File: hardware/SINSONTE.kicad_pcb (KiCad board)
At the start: 2 copper layers, 90 x 70 mm, 39 parts, among them J1 BAT, J10 Conn_01x01_Male, J11 Conn_01x01_Male, J12 Conn_01x04_Male, J13 Conn_01x01_Male, J14 Conn_01x02_Male, J2 CLOCK, J3 LIGHT_SENSOR, J4 Conn_01x17_Male, J5 Conn_01x01_Male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

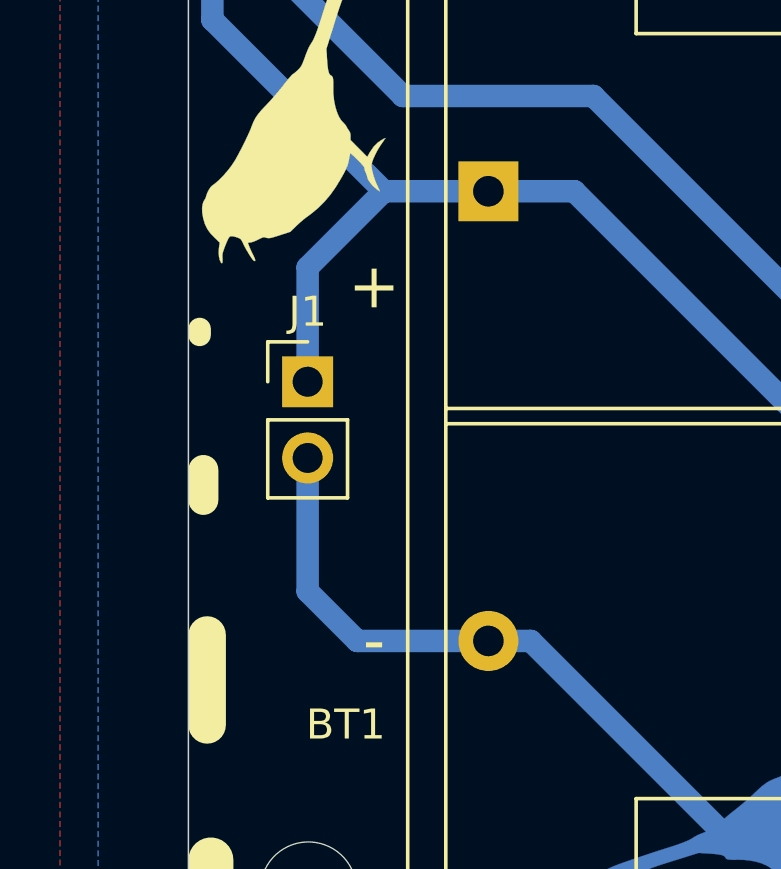
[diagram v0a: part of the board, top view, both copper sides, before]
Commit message: changed ext batt for screw terminal type
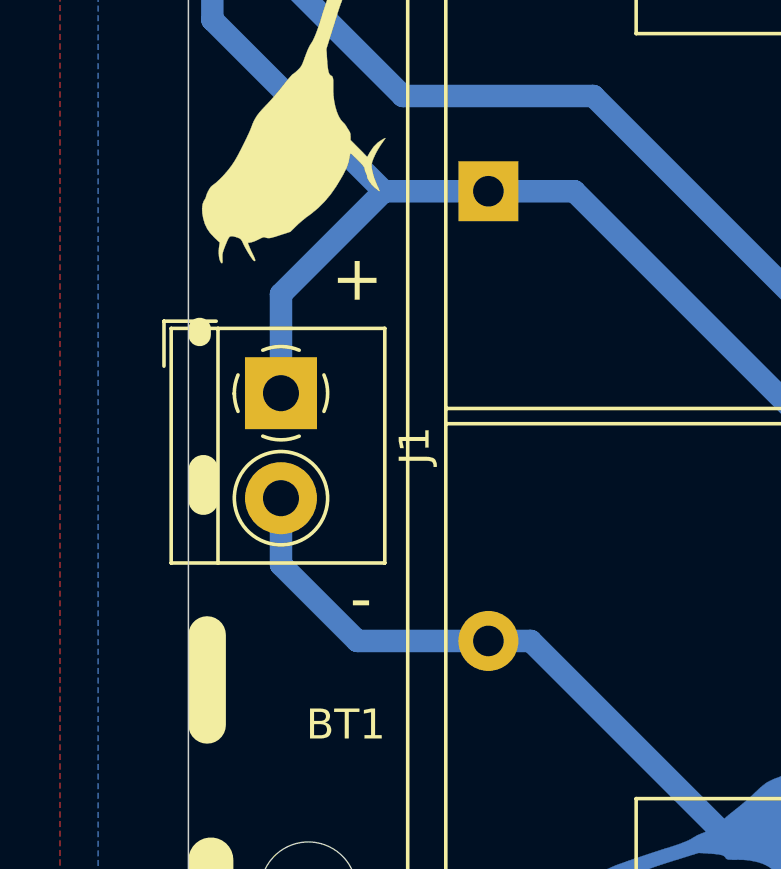
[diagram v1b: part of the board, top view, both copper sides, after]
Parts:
- J1: footprint Connector_PinHeader_2.54mm:PinHeader_1x02_P2.54mm_Vertical -> TerminalBlock_4Ucon:TerminalBlock_4Ucon_1x02_P3.50mm_Horizontal
- moved J1 0.97 mm to (53.1, 99.4), turned to 270 degrees
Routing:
- net Net-(BT1-Pad2): track 321.7 -> 320.7 mm
- net Net-(BT1-Pad1): track 124.6 -> 125.3 mm
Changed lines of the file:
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@@
     (add_net "Net-(U1-Pad43)")
+  )
+  (module TerminalBlock_4Ucon:TerminalBlock_4Ucon_1x02_P3.50mm_Horizontal (layer F.Cu)
+    (at 53.086 99.441 270)
+    (descr "Terminal Block 4Ucon ItemNo. 19963, 2 pins, pitch 3.5mm, size 7.7x7mm^2, drill diamater 1.2mm, pad diameter 2.4mm, see http://www.4uconnector.com/online/object/4udrawing/19963.pdf, script-generated using https://github.com/pointhi/kicad-footprint-generator/scripts/TerminalBlock_4Ucon")
+    (tags "THT Terminal Block 4Ucon ItemNo. 19963 pitch 3.5mm size 7.7x7mm^2 drill 1.2mm pad 2.4mm")
+    (fp_text reference J1 (at 1.75 -4.46 90) (layer F.SilkS)
+      (effects (font (size 1 1) (thickness 0.15)))
+    )
+    (fp_text value BAT (at 1.75 4.66 90) (layer F.Fab)
+      (effects (font (size 1 1) (thickness 0.15)))
+    )
+    (fp_text user %R (at 1.75 2.9 90) (layer F.Fab)
+      (effects (font (size 1 1) (thickness 0.15)))
+    )
+    (fp_line (start 6.1 -3.9) (end -2.6 -3.9) (layer F.CrtYd) (width 0.05))
+    (fp_line (start 6.1 4.1) (end 6.1 -3.9) (layer F.CrtYd) (width 0.05))
+    (fp_line (start -2.6 4.1) (end 6.1 4.1) (layer F.CrtYd) (width 0.05))
+    (fp_line (start -2.6 -3.9) (end -2.6 4.1) (layer F.CrtYd) (width 0.05))
+    (fp_line (start -2.4 3.9) (end -0.9 3.9) (layer F.SilkS) (width 0.12))
+    (fp_line (start -2.4 2.16) (end -2.4 3.9) (layer F.SilkS) (width 0.12))
+    (fp_line (start 2.4 0.069) (end 2.4 -0.069) (layer F.Fab) (width 0.1))
+    (fp_line (start 3.431 0.069) (end 2.4 0.069) (layer F.Fab) (width 0.1))
+    (fp_line (start 3.431 1.1) (end 3.431 0.069) (layer F.Fab) (width 0.1))
+    (fp_line (start 3.569 1.1) (end 3.431 1.1) (layer F.Fab) (width 0.1))
+    (fp_line (start 3.569 0.069) (end 3.569 1.1) (layer F.Fab) (width 0.1))
+    (fp_line (start 4.6 0.069) (end 3.569 0.069) (layer F.Fab) (width 0.1))
+    (fp_line (start 4.6 -0.069) (end 4.6 0.069) (layer F.Fab) (width 0.1))
+    (fp_line (start 3.569 -0.069) (end 4.6 -0.069) (layer F.Fab) (width 0.1))
+    (fp_line (start 3.569 -1.1) (end 3.569 -0.069) (layer F.Fab) (width 0.1))
+    (fp_line (start 3.431 -1.1) (end 3.569 -1.1) (layer F.Fab) (width 0.1))
+    (fp_line (start 3.431 -0.069) (end 3.431 -1.1) (layer F.Fab) (width 0.1))
+    (fp_line (start 2.4 -0.069) (end 3.431 -0.069) (layer F.Fab) (width 0.1))
+    (fp_line (start -1.1 0.069) (end -1.1 -0.069) (layer F.Fab) (width 0.1))
+    (fp_line (start -0.069 0.069) (end -1.1 0.069) (layer F.Fab) (width 0.1))
+    (fp_line (start -0.069 1.1) (end -0.069 0.069) (layer F.Fab) (width 0.1))
+    (fp_line (start 0.069 1.1) (end -0.069 1.1) (layer F.Fab) (width 0.1))
+    (fp_line (start 0.069 0.069) (end 0.069 1.1) (layer F.Fab) (width 0.1))
+    (fp_line (start 1.1 0.069) (end 0.069 0.069) (layer F.Fab) (width 0.1))
+    (fp_line (start 1.1 -0.069) (end 1.1 0.069) (layer F.Fab) (width 0.1))
+    (fp_line (start 0.069 -0.069) (end 1.1 -0.069) (layer F.Fab) (width 0.1))
+    (fp_line (start 0.069 -1.1) (end 0.069 -0.069) (layer F.Fab) (width 0.1))
+    (fp_line (start -0.069 -1.1) (end 0.069 -1.1) (layer F.Fab) (width 0.1))
+    (fp_line (start -0.069 -0.069) (end -0.069 -1.1) (layer F.Fab) (width 0.1))
+    (fp_line (start -1.1 -0.069) (end -0.069 -0.069) (layer F.Fab) (width 0.1))
+    (fp_line (start 5.66 -3.46) (end 5.66 3.66) (layer F.SilkS) (width 0.12))
+    (fp_line (start -2.16 -3.46) (end -2.16 3.66) (layer F.SilkS) (width 0.12))
+    (fp_line (start -2.16 3.66) (end 5.66 3.66) (layer F.SilkS) (width 0.12))
+    (fp_line (start -2.16 -3.46) (end 5.66 -3.46) (layer F.SilkS) (width 0.12))
+    (fp_line (start -2.16 2.1) (end 5.66 2.1) (layer F.SilkS) (width 0.12))
+    (fp_line (start -2.1 2.1) (end 5.6 2.1) (layer F.Fab) (width 0.1))
+    (fp_line (start -2.1 2.1) (end -2.1 -3.4) (layer F.Fab) (width 0.1))
+    (fp_line (start -0.6 3.6) (end -2.1 2.1) (layer F.Fab) (width 0.1))
+    (fp_line (start 5.6 3.6) (end -0.6 3.6) (layer F.Fab) (width 0.1))
+    (fp_line (start 5.6 -3.4) (end 5.6 3.6) (layer F.Fab) (width 0.1))
+    (fp_line (start -2.1 -3.4) (end 5.6 -3.4) (layer F.Fab) (width 0.1))
+    (fp_circle (center 3.5 0) (end 5.055 0) (layer F.SilkS) (width 0.12))
+    (fp_circle (center 3.5 0) (end 4.875 0) (layer F.Fab) (width 0.1))
+    (fp_circle (center 0 0) (end 1.375 0) (layer F.Fab) (width 0.1))
+    (fp_arc (start 0 0) (end -0.608 1.432) (angle -24) (layer F.SilkS) (width 0.12))
+    (fp_arc (start 0 0) (end -1.432 -0.608) (angle -46) (layer F.SilkS) (width 0.12))
+    (fp_arc (start 0 0) (end 0.608 -1.432) (angle -46) (layer F.SilkS) (width 0.12))
+    (fp_arc (start 0 0) (end 1.432 0.608) (angle -46) (layer F.SilkS) (width 0.12))
+    (fp_arc (start 0 0) (end 0 1.555) (angle -23) (layer F.SilkS) (width 0.12))
+    (pad 2 thru_hole circle (at 3.5 0 270) (size 2.4 2.4) (drill 1.2) (layers *.Cu *.Mask)
+      (net 4 "Net-(BT1-Pad2)"))
+    (pad 1 thru_hole rect (at 0 0 270) (size 2.4 2.4) (drill 1.2) (layers *.Cu *.Mask)
+      (net 5 "Net-(BT1-Pad1)"))
+    (model ${KISYS3DMOD}/TerminalBlock_4Ucon.3dshapes/TerminalBlock_4Ucon_1x02_P3.50mm_Horizontal.wrl
+      (at (xyz 0 0 0))
+      (scale (xyz 1 1 1))
+      (rotate (xyz 0 0 0))
+    )
   )
   (module Logos_Galopago:sinsonte_logo_11x6mm_cu (layer B.Cu)
@@
     )
   )
-  (module Connector_PinHeader_2.54mm:PinHeader_1x02_P2.54mm_Vertical (layer F.Cu)
-    (at 53.975 99.06)
-    (descr "Through hole straight pin header, 1x02, 2.54mm pitch, single row")
-    (tags "Through hole pin header THT 1x02 2.54mm single row")
-    (fp_text reference J1 (at 0 -2.33) (layer F.SilkS)
-      (effects (font (size 1 1) (thickness 0.15)))
-    )
-    (fp_text value BAT (at 0 4.87) (layer F.Fab)
-      (effects (font (size 1 1) (thickness 0.15)))
-    )
-    (fp_text user %R (at 0 1.27 90) (layer F.Fab)
-      (effects (font (size 1 1) (thickness 0.15)))
-    )
-    (fp_line (start 1.8 -1.8) (end -1.8 -1.8) (layer F.CrtYd) (width 0.05))
-    (fp_line (start 1.8 4.35) (end 1.8 -1.8) (layer F.CrtYd) (width 0.05))
-    (fp_line (start -1.8 4.35) (end 1.8 4.35) (layer F.CrtYd) (width 0.05))
-    (fp_line (start -1.8 -1.8) (end -1.8 4.35) (layer F.CrtYd) (width 0.05))
-    (fp_line (start -1.33 -1.33) (end 0 -1.33) (layer F.SilkS) (width 0.12))
-    (fp_line (start -1.33 0) (end -1.33 -1.33) (layer F.SilkS) (width 0.12))
-    (fp_line (start -1.33 1.27) (end 1.33 1.27) (layer F.SilkS) (width 0.12))
-    (fp_line (start 1.33 1.27) (end 1.33 3.87) (layer F.SilkS) (width 0.12))
-    (fp_line (start -1.33 1.27) (end -1.33 3.87) (layer F.SilkS) (width 0.12))
-    (fp_line (start -1.33 3.87) (end 1.33 3.87) (layer F.SilkS) (width 0.12))
-    (fp_line (start -1.27 -0.635) (end -0.635 -1.27) (layer F.Fab) (width 0.1))
-    (fp_line (start -1.27 3.81) (end -1.27 -0.635) (layer F.Fab) (width 0.1))
-    (fp_line (start 1.27 3.81) (end -1.27 3.81) (layer F.Fab) (width 0.1))
-    (fp_line (start 1.27 -1.27) (end 1.27 3.81) (layer F.Fab) (width 0.1))
-    (fp_line (start -0.635 -1.27) (end 1.27 -1.27) (layer F.Fab) (width 0.1))
-    (pad 2 thru_hole oval (at 0 2.54) (size 1.7 1.7) (drill 1) (layers *.Cu *.Mask)
-      (net 4 "Net-(BT1-Pad2)"))
-    (pad 1 thru_hole rect (at 0 0) (size 1.7 1.7) (drill 1) (layers *.Cu *.Mask)
-      (net 5 "Net-(BT1-Pad1)"))
-    (model ${KISYS3DMOD}/Connector_PinHeader_2.54mm.3dshapes/PinHeader_1x02_P2.54mm_Vertical.wrl
-      (at (xyz 0 0 0))
-      (scale (xyz 1 1 1))
-      (rotate (xyz 0 0 0))
-    )
-  )
   (module Battery:BatteryHolder_Keystone_2462_2xAA (layer F.Cu)
     (at 60 92.71)
@@
     (fp_line (start -2.84 24.21) (end 57.17 24.21) (layer F.CrtYd) (width 0.05))
     (fp_line (start 57.17 24.21) (end 57.17 -9.22) (layer F.CrtYd) (width 0.05))
-    (fp_text user - (at -3.81 14.99) (layer F.SilkS)
+    (fp_text user - (at -4.247 13.589) (layer F.SilkS)
       (effects (font (size 1.5 1.5) (thickness 0.15)))
     )
-    (fp_text user + (at -3.81 3.175) (layer F.SilkS)
+    (fp_text user + (at -4.374 2.921) (layer F.SilkS)
       (effects (font (size 1.5 1.5) (thickness 0.15)))
     )
@@
   (segment (start 71.65 80.43) (end 71.65 77.89) (width 0.75) (layer B.Cu) (net 4))
   (segment (start 58.95 80.43) (end 58.95 77.89) (width 0.75) (layer B.Cu) (net 4))
-  (segment (start 53.975 101.6) (end 53.975 106.045) (width 0.75) (layer B.Cu) (net 4))
-  (segment (start 53.975 106.045) (end 55.63 107.7) (width 0.75) (layer B.Cu) (net 4))
-  (segment (start 55.63 107.7) (end 60 107.7) (width 0.75) (layer B.Cu) (net 4))
-  (segment (start 53.975 99.06) (end 53.975 95.25) (width 0.75) (layer B.Cu) (net 5))
+  (segment (start 53.086 105.156) (end 53.086 102.941) (width 0.75) (layer B.Cu) (net 4))
+  (segment (start 55.63 107.7) (end 53.086 105.156) (width 0.75) (layer B.Cu) (net 4))
+  (segment (start 60 107.7) (end 55.63 107.7) (width 0.75) (layer B.Cu) (net 4))
   (segment (start 56.515 92.71) (end 60 92.71) (width 0.75) (layer B.Cu) (net 5))
-  (segment (start 53.975 95.25) (end 56.515 92.71) (width 0.75) (layer B.Cu) (net 5))
   (segment (start 56.41 60.11) (end 56.41 57.57) (width 0.75) (layer B.Cu) (net 5))
   (segment (start 110.25 100.965) (end 71.12 100.965) (width 0.75) (layer B.Cu) (net 5))
@@
   (segment (start 56.41 62.335) (end 55.245 63.5) (width 0.75) (layer B.Cu) (net 5))
   (segment (start 56.41 60.11) (end 56.41 62.335) (width 0.75) (layer B.Cu) (net 5))
+  (segment (start 53.086 96.139) (end 53.086 99.441) (width 0.75) (layer B.Cu) (net 5))
+  (segment (start 56.515 92.71) (end 53.086 96.139) (width 0.75) (layer B.Cu) (net 5))
   (segment (start 128 83.035) (end 128 89.535) (width 0.75) (layer B.Cu) (net 6))
   (segment (start 128 93.615) (end 129 94.615) (width 0.75) (layer B.Cu) (net 6))

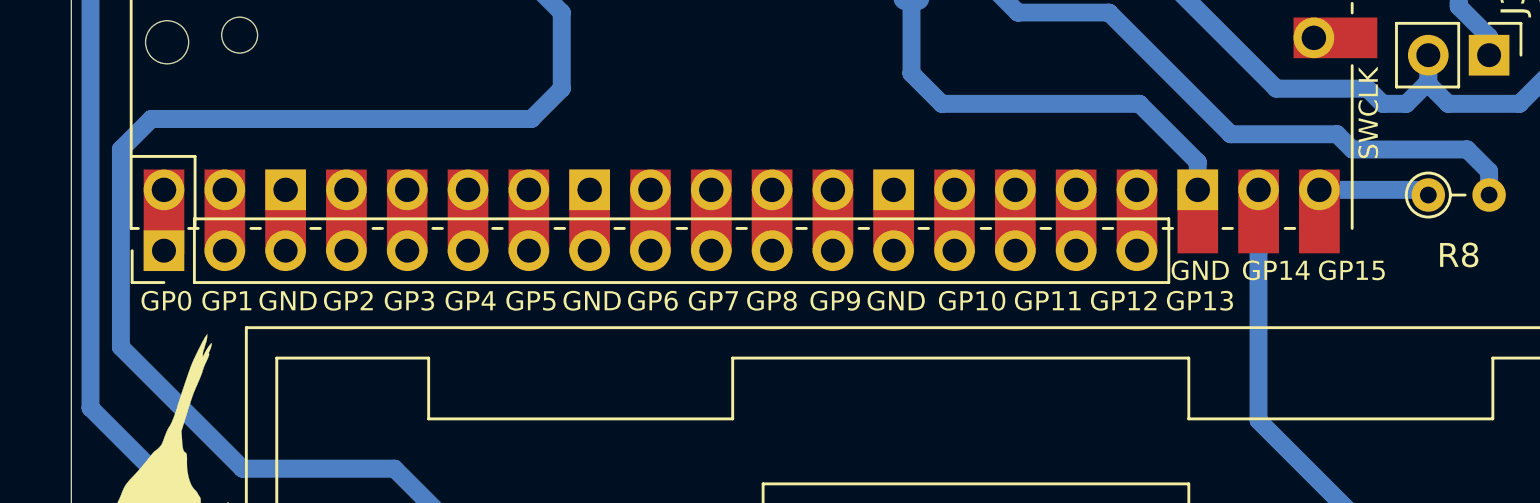
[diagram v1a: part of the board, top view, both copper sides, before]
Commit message: rpi first half conn aded 1 pos on ground
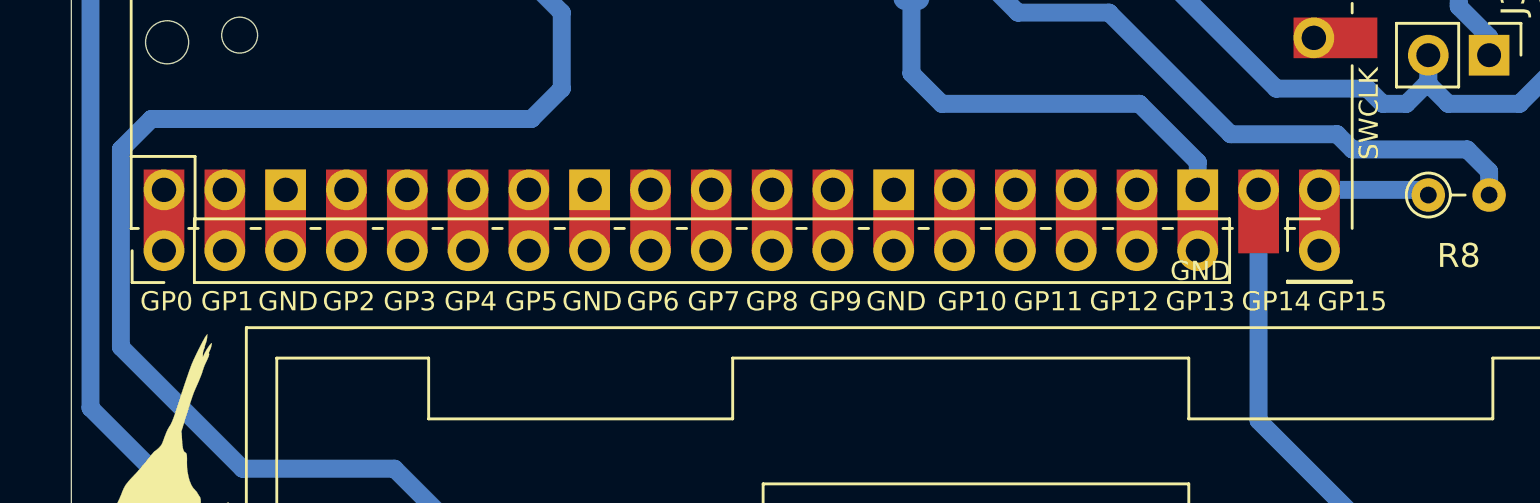
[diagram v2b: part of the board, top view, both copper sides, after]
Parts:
- added J15: Conn_01x01_Male, Connector_PinHeader_2.54mm:PinHeader_1x01_P2.54mm_Vertical, F.Cu at (102.1, 80.4)
- J4: value Conn_01x17_Male -> Conn_01x18_Male; footprint Connector_PinHeader_2.54mm:PinHeader_1x17_P2.54mm_Vertical -> Connector_PinHeader_2.54mm:PinHeader_1x18_P2.54mm_Vertical
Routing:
- net Net-(BT1-Pad2): track 320.7 -> 323.3 mm

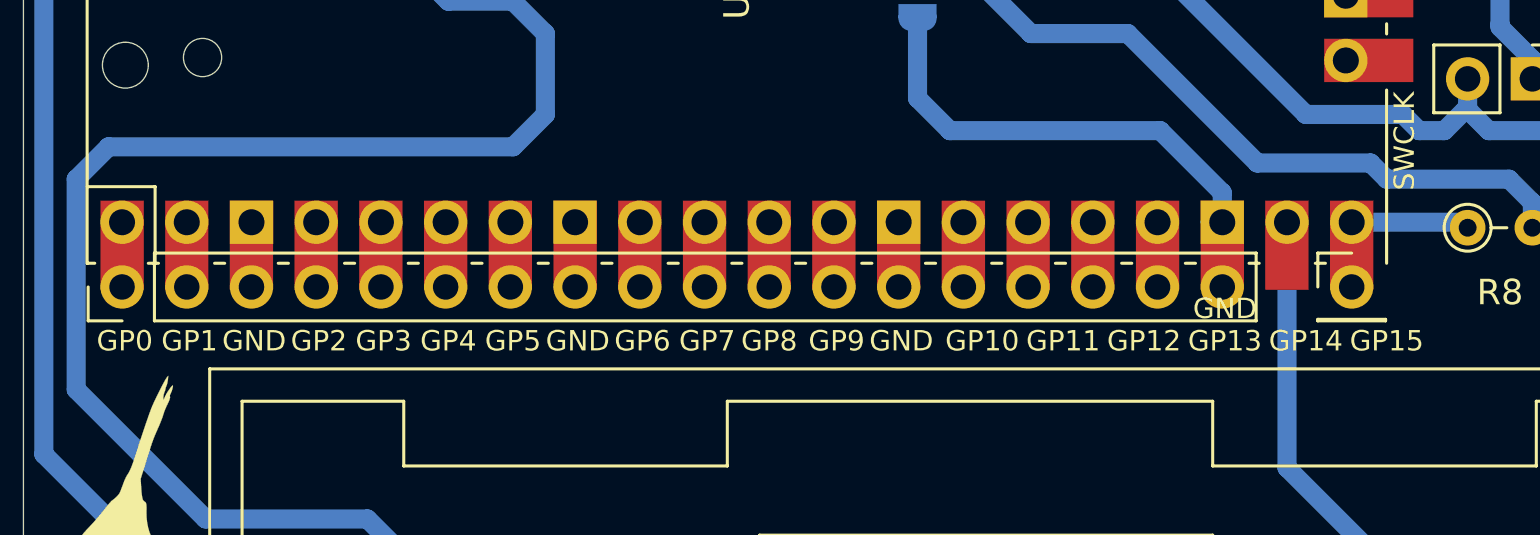
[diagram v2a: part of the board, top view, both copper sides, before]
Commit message: rpi first half conn aded all pins connector
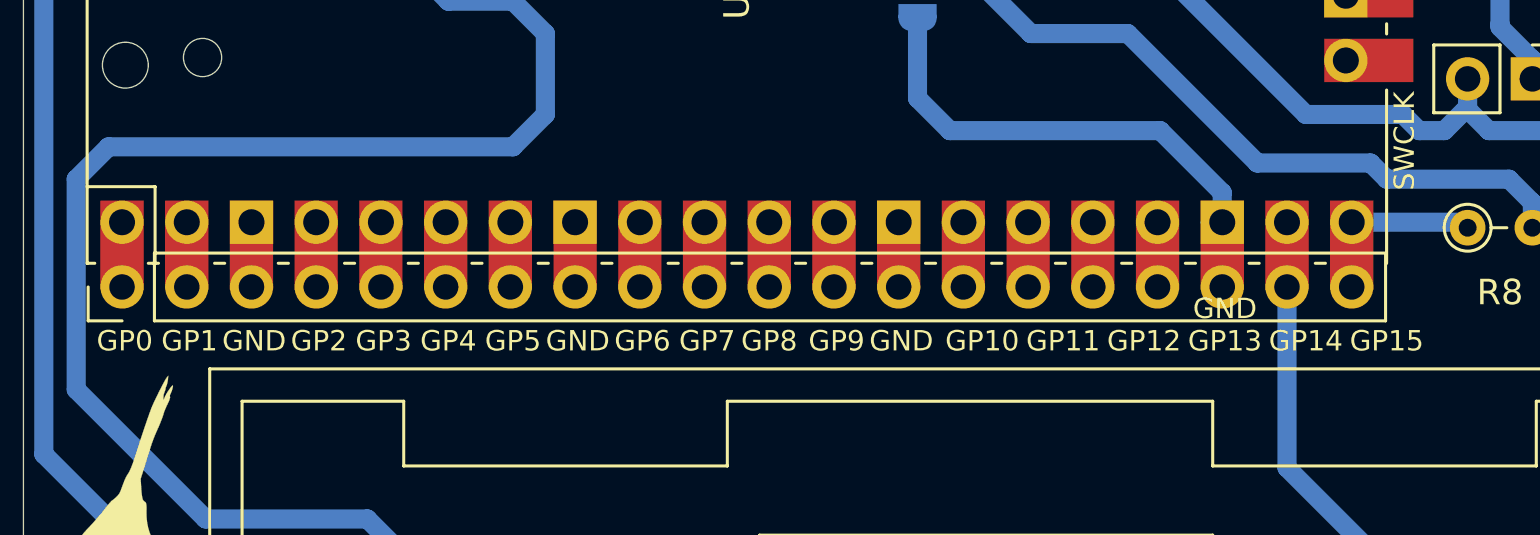
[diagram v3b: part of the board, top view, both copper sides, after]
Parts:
- removed J15: Conn_01x01_Male, Connector_PinHeader_2.54mm:PinHeader_1x01_P2.54mm_Vertical
- J4: value Conn_01x18_Male -> Conn_01x20_Male; footprint Connector_PinHeader_2.54mm:PinHeader_1x18_P2.54mm_Vertical -> Connector_PinHeader_2.54mm:PinHeader_1x20_P2.54mm_Vertical
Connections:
- R2 pad 1: Net-(R2-Pad1) -> Net-(J4-Pad19)
- R8 pad 1: Net-(J15-Pad1) -> Net-(J4-Pad20)
- U1 pad 19: Net-(R2-Pad1) -> Net-(J4-Pad19)
- U1 pad 20: Net-(J15-Pad1) -> Net-(J4-Pad20)
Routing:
- net Net-(R2-Pad1): track 36.8 -> 0.00 mm
- net Net-(J4-Pad19): track 0.00 -> 36.8 mm
- net Net-(J4-Pad20): track 0.00 -> 7.48 mm
- net Net-(J15-Pad1): track 4.94 -> 0.00 mm
